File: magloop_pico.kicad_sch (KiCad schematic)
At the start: 102 parts, among them J1 Conn_Coaxial_Power, J10 5V AUDIO MUTE, J2 Conn_02x03_Odd_Even, J3 POWER SW, J4 Conn_02x03_Odd_Even, J5 Conn_02x04_Odd_Even, J6 TO RF RELAY, J7 ETHERNET, J8 5-1634513-1, J9 12V AUDIO MUTE, Q1 NPN, Q10 PMOS, Q11 NPN, Q12 PMOS, Q2 NPN, Q3 NPN, Q4 NPN, Q5 NPN, Q6 NPN, Q7 NPN, Q8 PMOS, Q9 NPN, SW1 SW_DIP_x03, U1 AD9850MODULE, U2 TMC2209_Module, U3 LM7805, U4 PI_PICO, U5 LM4040DBZ-3, U7 LM358, U8 LM358

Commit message: Got all nets wired. Not clean yet.
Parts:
- removed R34, R39: 10K, Resistor_SMD:R_1206_3216Metric_Pad1.30x1.75mm_HandSolder, symbol Device:R_US
- removed SW1: SW_DIP_x03, digikey-footprints:DIP-6_W7.62mm, symbol Switch:SW_DIP_x03
- added D7, D8: 1N4004, Diode_SMD:D_SMB, symbol Diode:1N4004
- Q1, Q10, Q11, Q12, Q2, Q3, Q4, Q5, Q6, Q7, Q8, Q9, U5: footprint Package_TO_SOT_SMD:SOT-23_Handsoldering -> Package_TO_SOT_SMD:SOT-23
- U1: footprint magloop_pico:AD9850_MODULE -> AD9850:AD9850_MODULE
- U2: footprint (none) -> TMC2209:TMC2209_MODULE
- U4: footprint magloop_pico:PI_PICO -> PI_Pico:PI_PICO
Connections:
- net GND: now also D8.2 (A)
- net at Q12.1 (G), R38.2: now also Q11.3 (C)
- net at C20.1, J6.2: now also D7.1 (K), D8.1 (K); no longer Q12.3 (D)
- net at Q7.3 (C): now also Q8.1 (G), R33.2
- net +3V3 renamed +3.3V
- new net: D7.2 (A), Q12.3 (D)
- no-connect marks 17 -> 19
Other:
- note added: "The enable resistor may not be necessary with UART control."
- note removed: "The DIP switches set stepper resolution."
- moved on the sheet: C20, J2, J6

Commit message: This commit prior to experiment re-ordering schematic designators.
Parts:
- U7, U8: footprint Package_DIP:DIP-8_W7.62mm -> Package_SO:SOIC-8_3.9x4.9mm_P1.27mm
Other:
- note added: "Pins 9 and 10 are ground tabs on the connector shell"
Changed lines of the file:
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@@
     (effects (font (size 0.9906 0.9906)) (justify left bottom))
+  )
+  (text "Pins 9 and 10 are\nground tabs on the\nconnector shell"
+    (at 38.1 158.115 0)
+    (effects (font (size 1 1)) (justify left bottom))
   )
   (text "These capacitors may" (at 78.105 120.65 0)
@@
       (effects (font (size 1.27 1.27)))
     )
-    (property "Footprint" "Package_DIP:DIP-8_W7.62mm" (at 201.93 27.94 0)
+    (property "Footprint" "Package_SO:SOIC-8_3.9x4.9mm_P1.27mm" (at 201.93 27.94 0)
       (effects (font (size 1.27 1.27)) hide)
     )
@@
       (effects (font (size 1.27 1.27)))
     )
-    (property "Footprint" "Package_DIP:DIP-8_W7.62mm" (at 238.76 64.77 0)
+    (property "Footprint" "Package_SO:SOIC-8_3.9x4.9mm_P1.27mm" (at 238.76 64.77 0)
       (effects (font (size 1.27 1.27)) hide)
     )
@@
       (effects (font (size 1.27 1.27)) (justify left))
     )
-    (property "Footprint" "Package_DIP:DIP-8_W7.62mm" (at 261.62 73.66 0)
+    (property "Footprint" "Package_SO:SOIC-8_3.9x4.9mm_P1.27mm" (at 261.62 73.66 0)
       (effects (font (size 1.27 1.27)) hide)
     )
@@
       (effects (font (size 1.27 1.27)))
     )
-    (property "Footprint" "Package_DIP:DIP-8_W7.62mm" (at 201.93 62.23 0)
+    (property "Footprint" "Package_SO:SOIC-8_3.9x4.9mm_P1.27mm" (at 201.93 62.23 0)
       (effects (font (size 1.27 1.27)) hide)
     )
@@
       (effects (font (size 1.27 1.27)))
     )
-    (property "Footprint" "Package_DIP:DIP-8_W7.62mm" (at 240.03 25.4 0)
+    (property "Footprint" "Package_SO:SOIC-8_3.9x4.9mm_P1.27mm" (at 240.03 25.4 0)
       (effects (font (size 1.27 1.27)) hide)
     )
@@
       (effects (font (size 1.27 1.27)) (justify left))
     )
-    (property "Footprint" "Package_DIP:DIP-8_W7.62mm" (at 262.89 30.48 0)
-      (effects (font (size 1.27 1.27)) hide)
-    )
+    (property "Footprint" "Package_SO:SOIC-8_3.9x4.9mm_P1.27mm" (at 262.89 30.48 0)
+      (effects (font (size 1.27 1.27)) hide)
+    )

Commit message: Seems to be clean. Wait another 24 hours before release.
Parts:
- renumbered C28 to C1, C26 to C10, C27 to C11, C21 to C12, C22 to C13, C6 to C14, C7 to C15, C8 to C16, C9 to C17, C10 to C18, C11 to C19, C1 to C2, C12 to C20, C13 to C21, C29 to C22, C24 to C23, C14 to C24, C20 to C25, C15 to C26, C16 to C27, C17 to C28, C18 to C29, C19 to C3, C3 to C4, C4 to C5, C2 to C6, C25 to C7, C23 to C8, C5 to C9, D6 to D1, D1 to D2, D2 to D3, D3 to D4, D8 to D5, D7 to D6, D4 to D7, D5 to D8, J2 to J10, J7 to J2, J9 to J4, J8 to J5, J10 to J6, J6 to J7, J4 to J8, J5 to J9, Q7 to Q3, Q3 to Q4, Q8 to Q5, Q4 to Q6, Q5 to Q7, Q6 to Q8, R8 to R10, R9 to R11, R10 to R12, R14 to R13, R13 to R14, R35 to R15, R15 to R16, R16 to R17, R36 to R18, R18 to R19, R17 to R20, R37 to R21, R21 to R22, R38 to R23, R20 to R24, R23 to R25, R22 to R26, R30 to R27, R31 to R28, R25 to R29, R24 to R30, R26 to R31, R27 to R32, R28 to R33, R29 to R34, R32 to R4, R4 to R5, R5 to R6, R6 to R7, R33 to R8, R7 to R9, U8 to U6

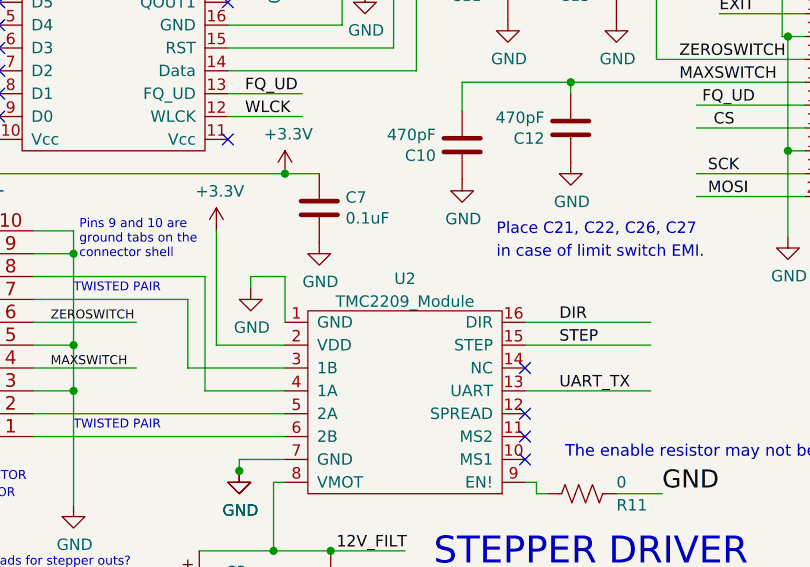
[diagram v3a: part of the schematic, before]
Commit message: Fixed BOM problem with R5.
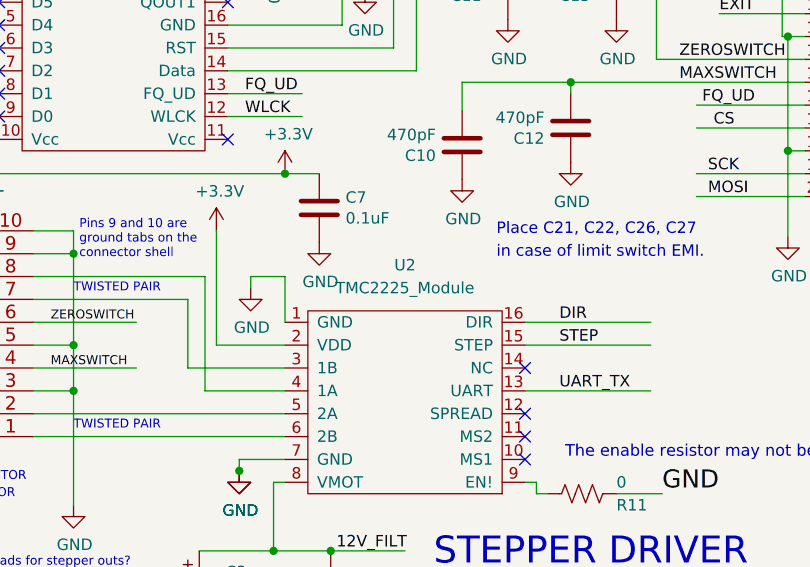
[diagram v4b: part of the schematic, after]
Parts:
- U2: value TMC2209_Module -> TMC2225_Module
